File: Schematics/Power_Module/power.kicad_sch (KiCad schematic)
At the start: 76 parts, among them J2 ScrewSwitch, J3 Battery, J6 ScrewSwitch, J7 GSE, Q1 AO4447A, Q2 AO4447A, Q3 AO3400A, Q4 AO3400A, U1 LMR51430YDDCR, U10 TPS61175PWPR, U14 LM74700QDBVRQ1, U15 LM74700QDBVRQ1, U2 LMR51430YDDCR, U3 ACS37041KLHBLT-010B3, U4 AMS1117-3.3, U5 ACS37041KLHBLT-010B3, U6 LM66100DCKR, U7 LM66100DCKR, U8 LM66100DCKR

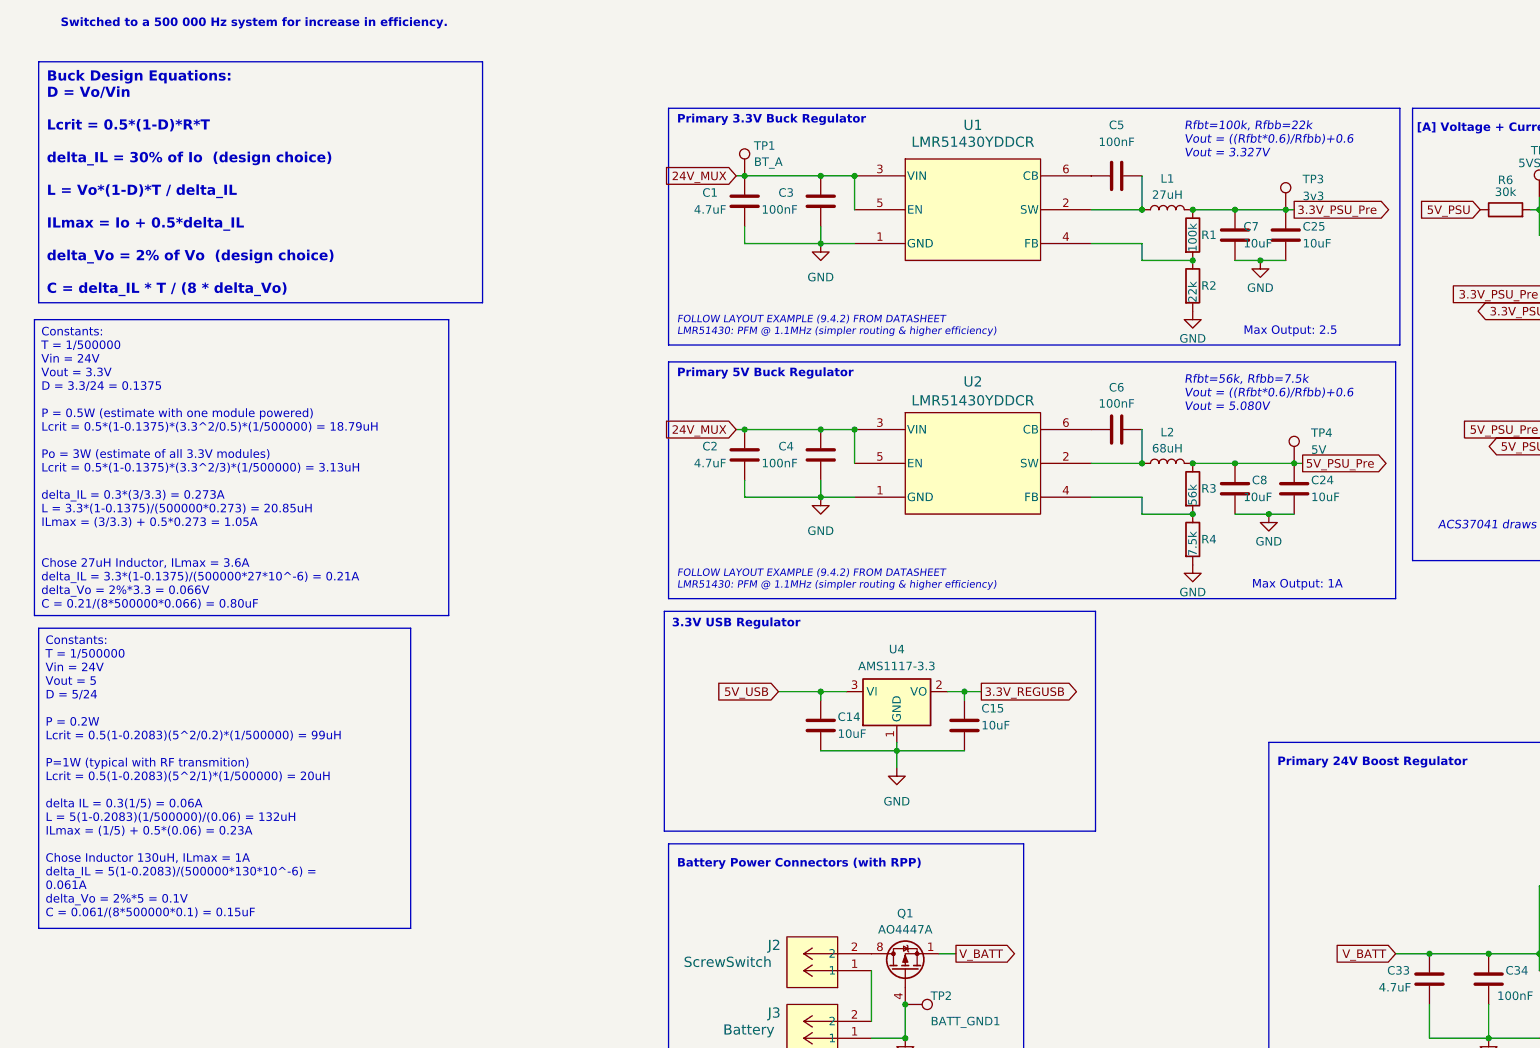
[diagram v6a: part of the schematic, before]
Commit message: Update buck designs for 500kHz, prioritize efficiency
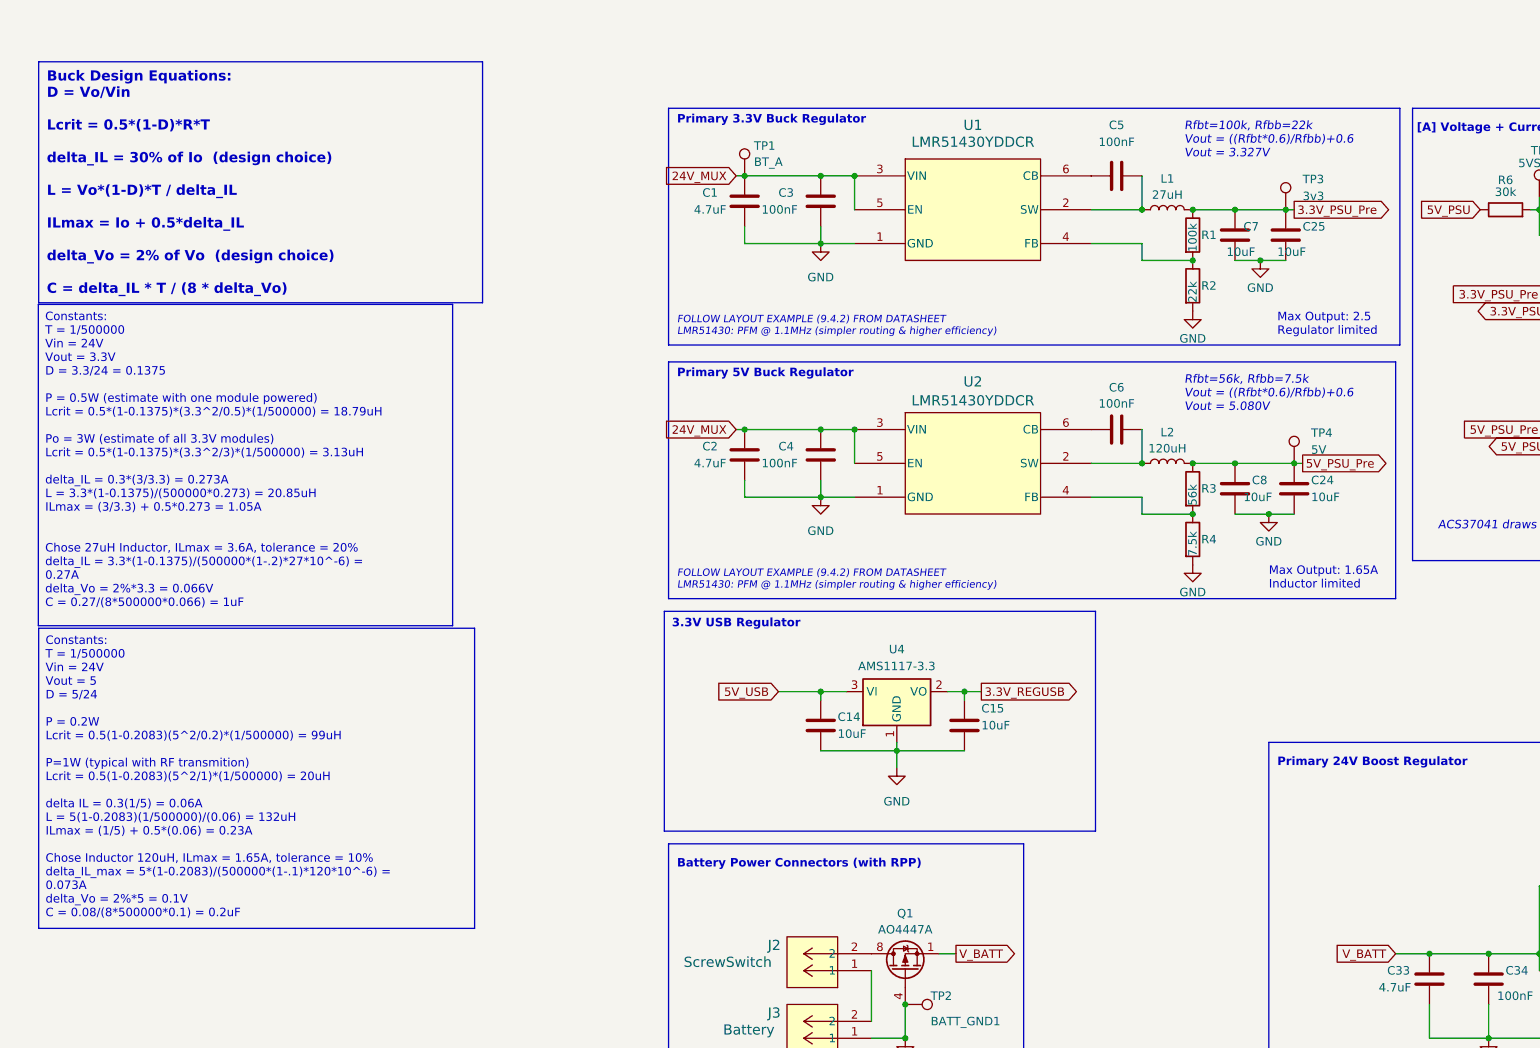
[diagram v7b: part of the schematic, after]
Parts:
- L1: footprint footprints:IND_VLS5045EX-100M-H -> Inductor_SMD:L_Bourns_SRR1260
- L2: value 68uH -> 120uH; footprint footprints:IND_VLS6045EX-680M-H -> Inductor_SMD:L_Bourns_SRR1260; Digikey 445-VLS6045EX-680M-HCT-ND -> SRR1260A-121KCT-ND
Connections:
- net 3.3V_PSU_Pre: now also L1.1; no longer L1.2
- net at C5.2, U1.2 (SW): now also L1.2; no longer L1.1
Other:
- note added: "Max Output: 1.65A Inductor limited"
- note added: "Max Output: 2.5 Regulator limited"
- note removed: "Max Output: 1A"
- note removed: "Max Output: 2.5"
- note removed: "Switched to a 500 000 Hz system for increase in efficiency."
- moved on the sheet: L1
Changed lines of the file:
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@@
 		)
 	)
-	(text_box "Constants:\nT = 1/500000\nVin = 24V\nVout = 5\nD = 5/24\n\nP = 0.2W\nLcrit = 0.5(1-0.2083)(5^2/0.2)*(1/500000) = 99uH\n\nP=1W (typical with RF transmition)\nLcrit = 0.5(1-0.2083)(5^2/1)*(1/500000) = 20uH\n\ndelta IL = 0.3(1/5) = 0.06A\nL = 5(1-0.2083)(1/500000)/(0.06) = 132uH\nILmax = (1/5) + 0.5*(0.06) = 0.23A\n\nChose Inductor 130uH, ILmax = 1A\ndelta_IL = 5(1-0.2083)/(500000*130*10^-6) = 0.061A\ndelta_Vo = 2%*5 = 0.1V\nC = 0.061/(8*500000*0.1) = 0.15uF"
+	(text_box "Constants:\nT = 1/500000\nVin = 24V\nVout = 5\nD = 5/24\n\nP = 0.2W\nLcrit = 0.5(1-0.2083)(5^2/0.2)*(1/500000) = 99uH\n\nP=1W (typical with RF transmition)\nLcrit = 0.5(1-0.2083)(5^2/1)*(1/500000) = 20uH\n\ndelta IL = 0.3(1/5) = 0.06A\nL = 5(1-0.2083)(1/500000)/(0.06) = 132uH\nILmax = (1/5) + 0.5*(0.06) = 0.23A\n\nChose Inductor 120uH, ILmax = 1.65A, tolerance = 10%\ndelta_IL_max = 5*(1-0.2083)/(500000*(1-.1)*120*10^-6) = 0.073A\ndelta_Vo = 2%*5 = 0.1V\nC = 0.08/(8*500000*0.1) = 0.2uF"
 		(exclude_from_sim no)
 		(at -80.645 93.345 0)
-		(size 55.88 45.085)
+		(size 65.4812 45.085)
 		(stroke
 			(width 0)
@@
 		)
 	)
-	(text_box "Constants:\nT = 1/500000\nVin = 24V\nVout = 3.3V\nD = 3.3/24 = 0.1375\n\nP = 0.5W (estimate with one module powered)\nLcrit = 0.5*(1-0.1375)*(3.3^2/0.5)*(1/500000) = 18.79uH\n\nPo = 3W (estimate of all 3.3V modules)\nLcrit = 0.5*(1-0.1375)*(3.3^2/3)*(1/500000) = 3.13uH\n\ndelta_IL = 0.3*(3/3.3) = 0.273A\nL = 3.3*(1-0.1375)/(500000*0.273) = 20.85uH\nILmax = (3/3.3) + 0.5*0.273 = 1.05A\n\n\nChose 27uH Inductor, ILmax = 3.6A \ndelta_IL = 3.3*(1-0.1375)/(500000*27*10^-6) = 0.21A\ndelta_Vo = 2%*3.3 = 0.066V\nC = 0.21/(8*500000*0.066) = 0.80uF"
+	(text_box "Constants:\nT = 1/500000\nVin = 24V\nVout = 3.3V\nD = 3.3/24 = 0.1375\n\nP = 0.5W (estimate with one module powered)\nLcrit = 0.5*(1-0.1375)*(3.3^2/0.5)*(1/500000) = 18.79uH\n\nPo = 3W (estimate of all 3.3V modules)\nLcrit = 0.5*(1-0.1375)*(3.3^2/3)*(1/500000) = 3.13uH\n\ndelta_IL = 0.3*(3/3.3) = 0.273A\nL = 3.3*(1-0.1375)/(500000*0.273) = 20.85uH\nILmax = (3/3.3) + 0.5*0.273 = 1.05A\n\n\nChose 27uH Inductor, ILmax = 3.6A, tolerance = 20%\ndelta_IL = 3.3*(1-0.1375)/(500000*(1-.2)*27*10^-6) = 0.27A\ndelta_Vo = 2%*3.3 = 0.066V\nC = 0.27/(8*500000*0.066) = 1uF"
 		(exclude_from_sim no)
-		(at -81.28 46.99 0)
-		(size 62.23 44.45)
+		(at -80.6958 44.704 0)
+		(size 62.23 48.26)
 		(stroke
 			(width 0)
@@
 		)
 	)
-	(text "Max Output: 2.5"
+	(text "Max Output: 2.5\nRegulator limited"
 		(exclude_from_sim no)
-		(at 100.33 49.53 0)
+		(at 105.41 49.53 0)
 		(effects
 			(font
@@
 		)
 	)
-	(text "Switched to a 500 000 Hz system for increase in efficiency."
-		(exclude_from_sim no)
-		(at -48.26 2.54 0)
-		(effects
-			(font
-				(size 1.27 1.27)
-				(thickness 0.254)
-				(bold yes)
-			)
-		)
-	)
 	(text "Battery Power Connectors (with RPP)"
 		(exclude_from_sim no)
@@
 		)
 	)
-	(text "Max Output: 1A"
+	(text "Max Output: 1.65A\nInductor limited"
 		(exclude_from_sim no)
-		(at 101.6 87.63 0)
+		(at 104.14 87.63 0)
 		(effects
 			(font
@@
 		)
 		(property "Value" "10uF"
-			(at 109.22 35.56 0)
+			(at 105.41 36.83 0)
 			(effects
 				(font
@@
 		)
 		(property "Value" "10uF"
-			(at 100.33 35.56 0)
+			(at 97.79 36.83 0)
 			(effects
 				(font
@@
 			)
 		)
-		(property "Value" "68uH"
+		(property "Value" "120uH"
 			(at 88.9 66.3546 90)
 			(effects
@@
 			)
 		)
-		(property "Footprint" "footprints:IND_VLS6045EX-680M-H"
+		(property "Footprint" "Inductor_SMD:L_Bourns_SRR1260"
 			(at 88.9 68.58 0)
 			(effects
@@
 			)
 		)
-		(property "Datasheet" "${KIPRJMOD}/../../Datasheets/inductor_vls5045ex-h"
+		(property "Datasheet" "${KIPRJMOD}/../../Datasheets/SRR1260A.pdf"
 			(at 88.9 68.58 0)
 			(effects
@@
 			)
 		)
-		(property "Digikey" "445-VLS6045EX-680M-HCT-ND"
+		(property "Digikey" "SRR1260A-121KCT-ND"
 			(at 88.9 68.58 90)
 			(effects
@@
 	(symbol
 		(lib_id "Device:L")
-		(at 88.9 30.48 90)
+		(at 88.9 30.48 270)
+		(mirror x)
 		(unit 1)
 		(exclude_from_sim no)
@@
 			)
 		)
-		(property "Footprint" "footprints:IND_VLS5045EX-100M-H"
+		(property "Footprint" "Inductor_SMD:L_Bourns_SRR1260"
 			(at 88.9 30.48 0)
 			(effects
@@
 			)
 		)
-		(property "Datasheet" "https://www.bourns.com/docs/Product-Datasheets/SRR1260A.pdf"
+		(property "Datasheet" "${KIPRJMOD}/../../Datasheets/SRR1260A.pdf"
 			(at 88.9 30.48 0)
 			(effects

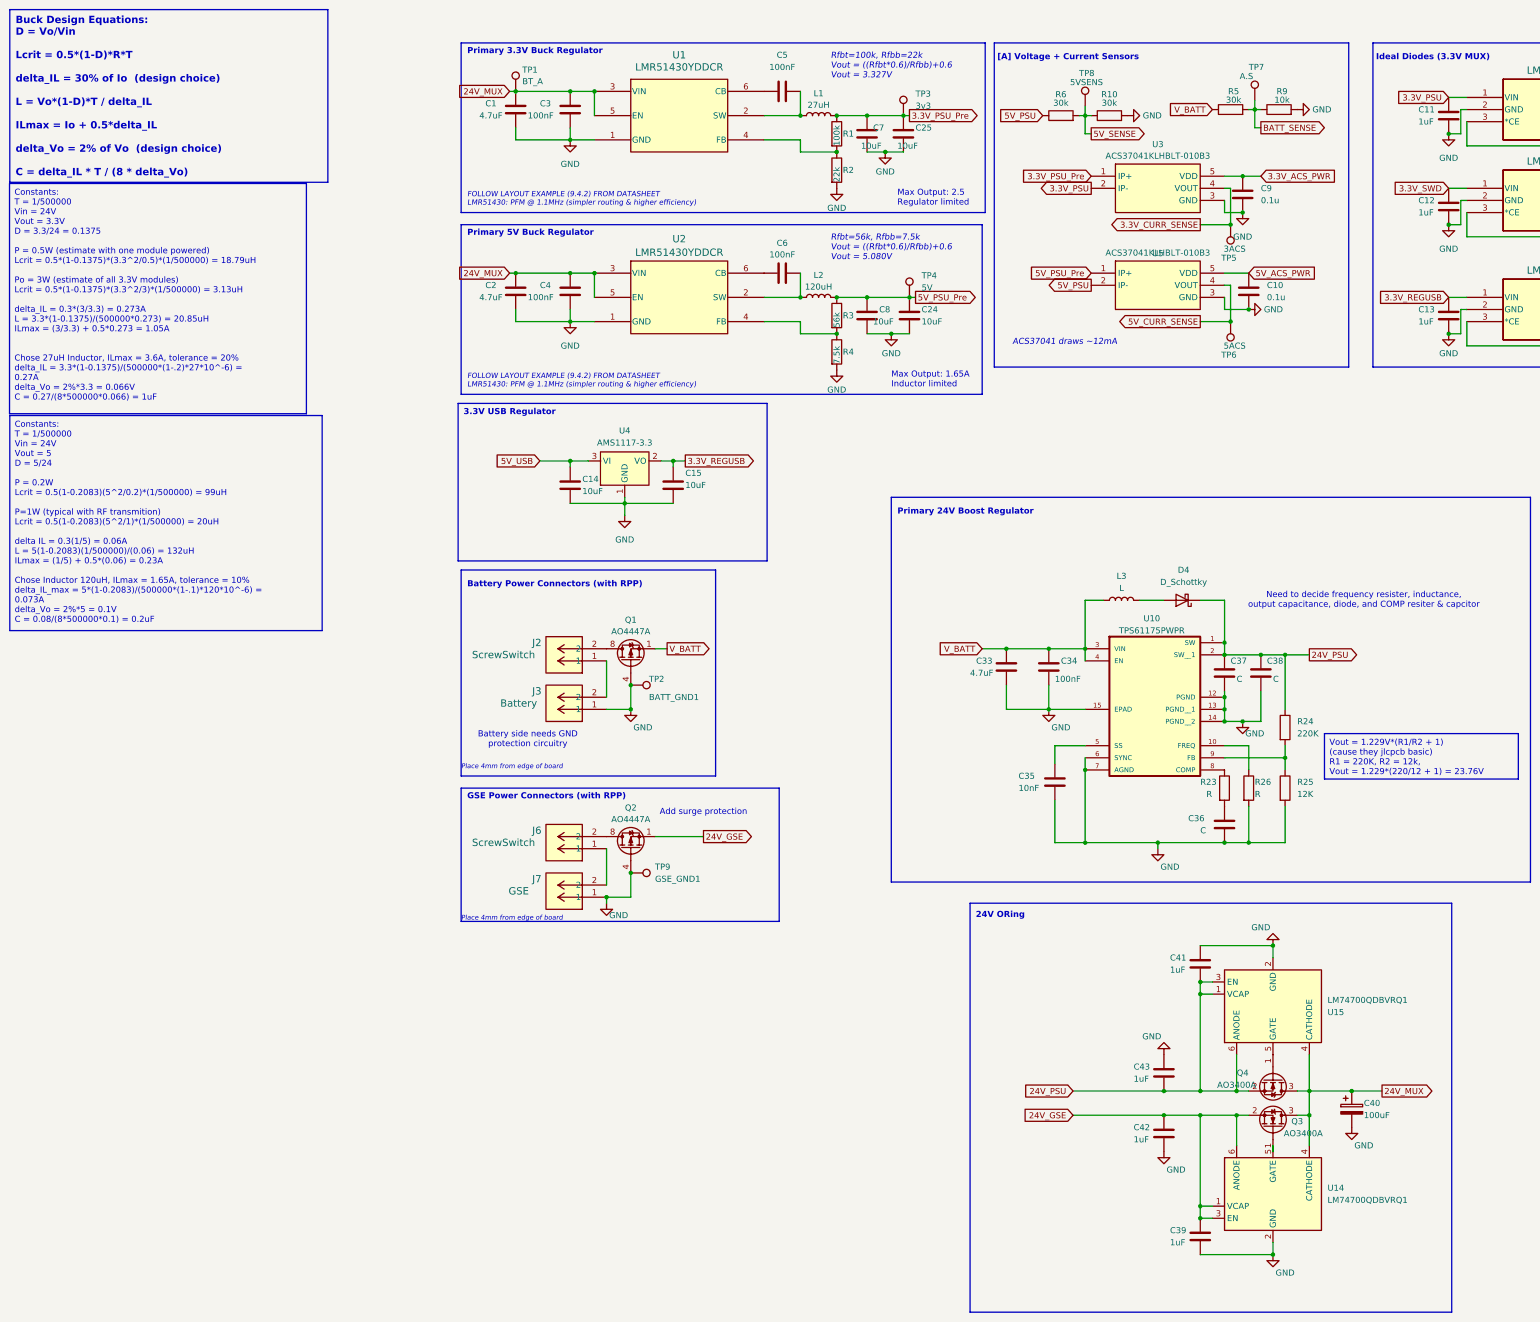
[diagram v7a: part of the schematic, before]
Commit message: updated buck input caps voltage rating to 50V
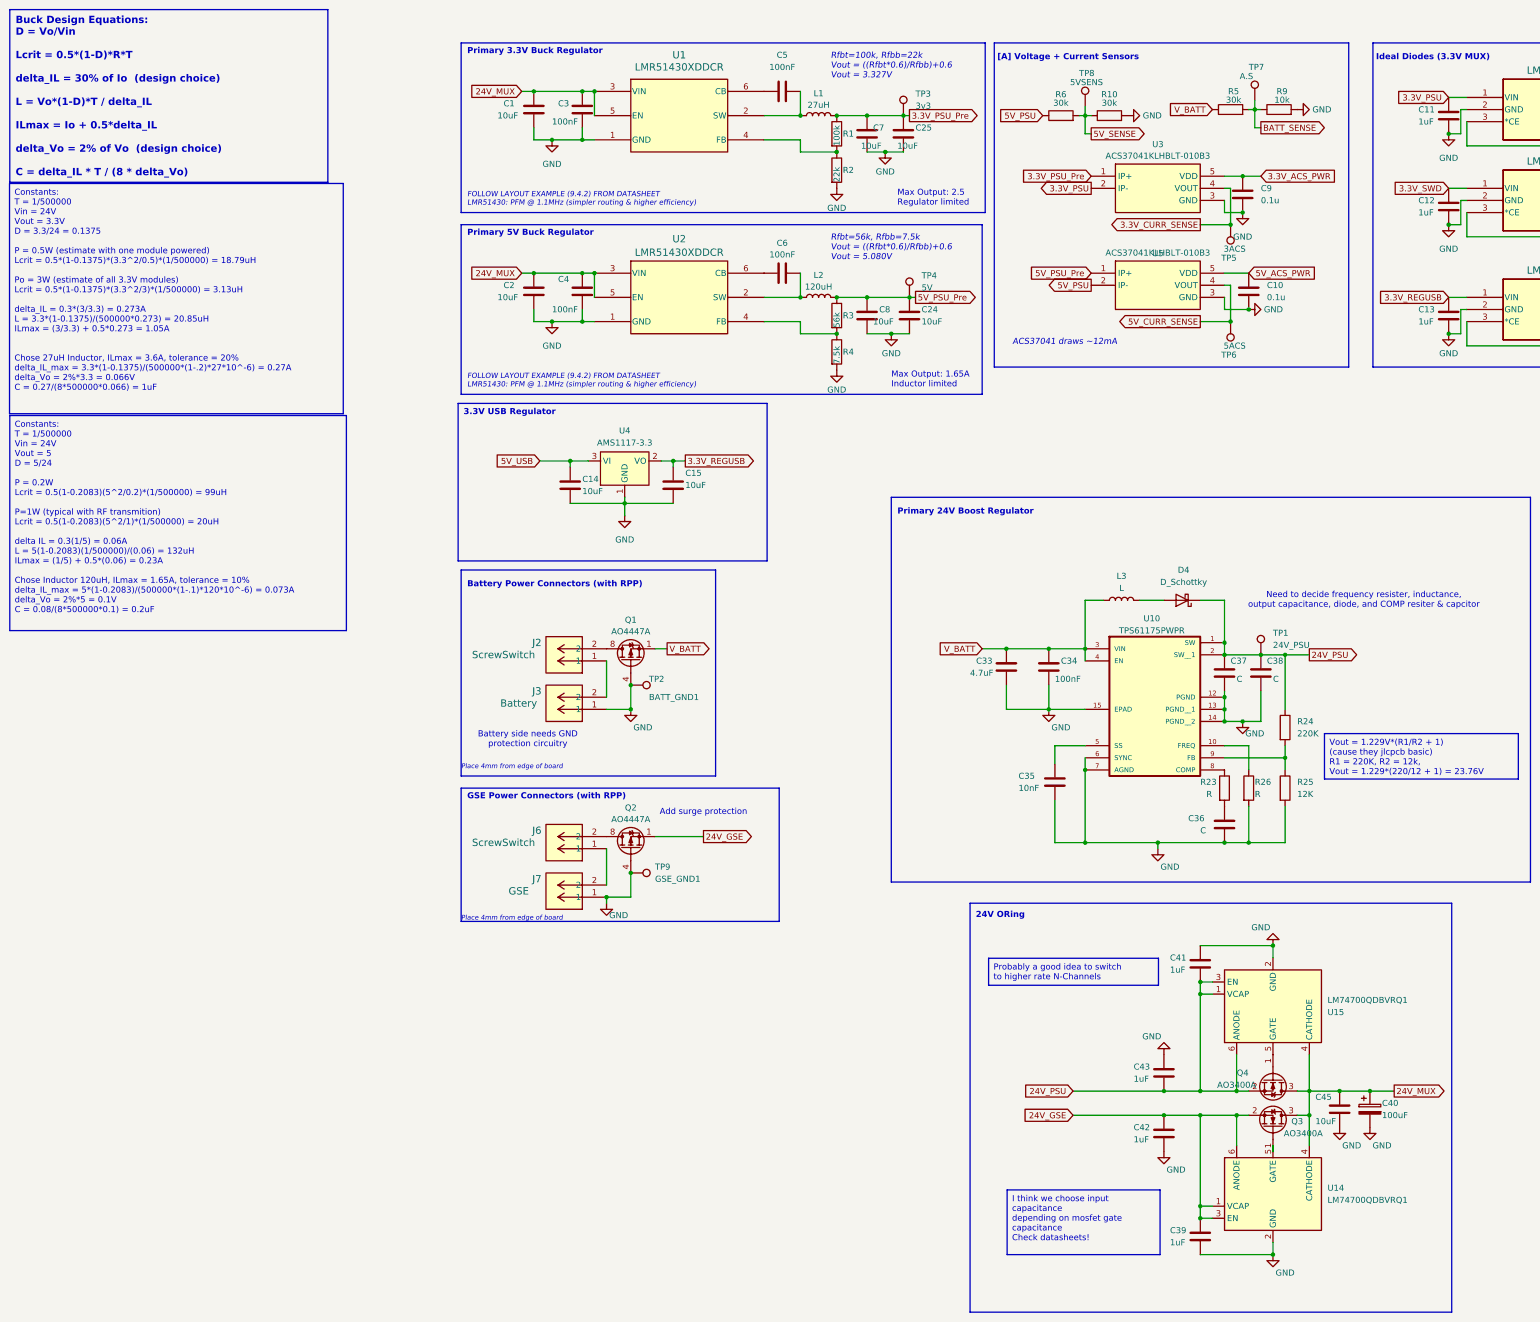
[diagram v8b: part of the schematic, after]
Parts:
- added C45: 10uF, Capacitor_SMD:C_1206_3216Metric, symbol Device:C
- C1, C2: value 4.7uF -> 10uF; footprint Capacitor_SMD:C_0805_2012Metric -> Capacitor_SMD:C_1206_3216Metric; JLCPCB C1779 -> C13585
- C40: footprint (none) -> Capacitor_SMD:CP_Elec_6.3x5.9
- TP1: value BT_A -> 24V_PSU
- U1, U2: value LMR51430YDDCR -> LMR51430XDDCR; LCSC C5210749 -> C5185863; _Digikey 296-LMR51430YDDCRCT-ND -> 296-LMR51430XDDCRCT-ND
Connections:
- net 24V_MUX: now also C45.1; no longer TP1.1
- net 24V_PSU: now also TP1.1
- net GND: now also C45.2
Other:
- moved on the sheet: C1, C3, C40
